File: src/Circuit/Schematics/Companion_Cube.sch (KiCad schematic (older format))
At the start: 13 parts

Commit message: Better origins on models
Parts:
- added D?: LED, ~, symbol LED
- added R?: R, ~, symbol R
- C?: value 10uF -> 1uF
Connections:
- net GND: now also R?.1
- net VCC: now also D?.1 (A)
- new net: D?.2 (K), R?.2
- no-connect marks 0 -> 3
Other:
- moved on the sheet: C?, CON?, IC?, P?, R?, RG?, U?

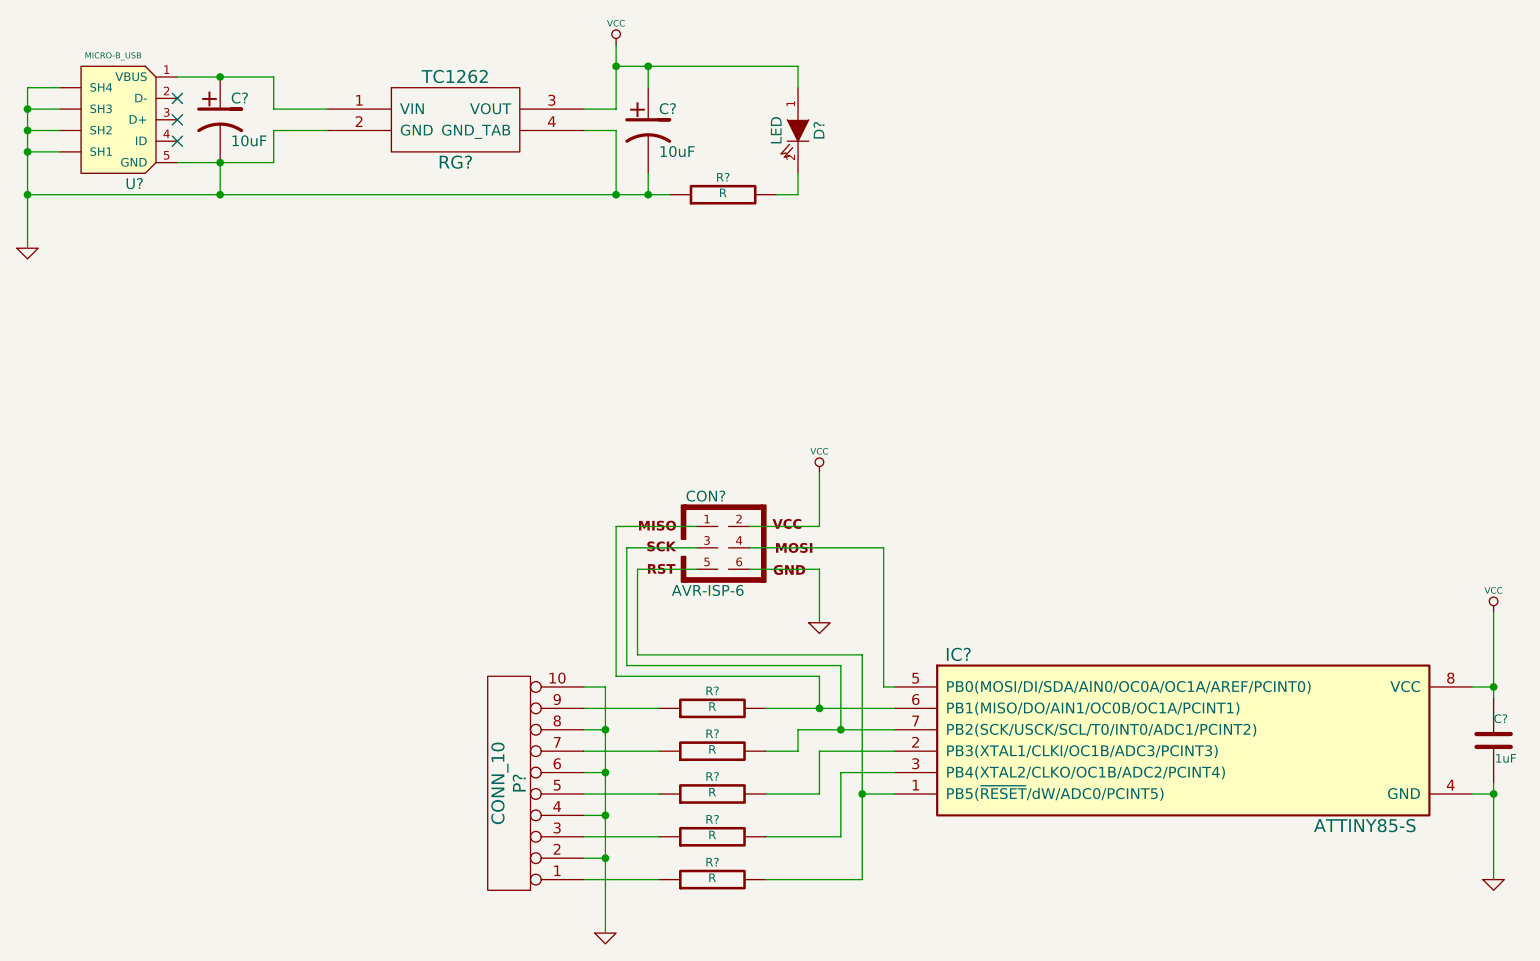
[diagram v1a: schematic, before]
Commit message: Removed use of reset pin from LED controller
The walls of the lid have also been shortened for slightly quicker
printing.
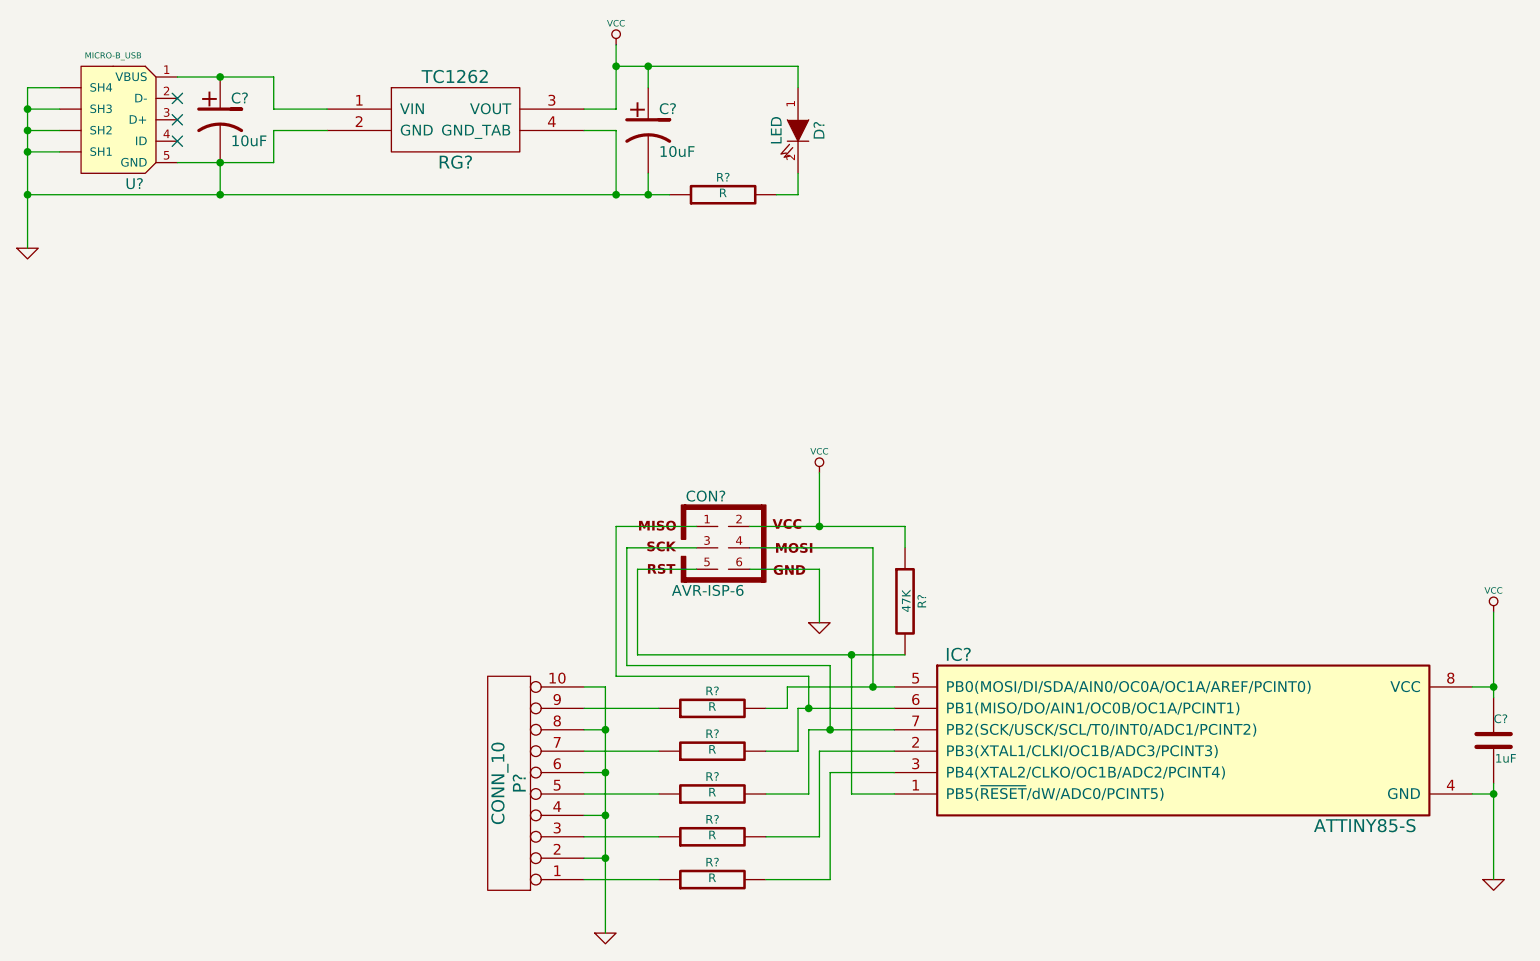
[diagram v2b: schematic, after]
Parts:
- added R?: 47K, ~, symbol R
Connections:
- net VCC: now also R?.1
- net at CON?.5, IC?.1 (PB5(~RESET~/dW/ADC0/PCINT5)): now also R?.2; no longer R?.2
- net at IC?.2 (PB3(XTAL1/CLKI/OC1B/ADC3/PCINT3)): now also R?.2; no longer R?.2
- net at IC?.3 (PB4(XTAL2/CLKO/OC1B/ADC2/PCINT4)): now also R?.2; no longer R?.2
- net at CON?.4, IC?.5 (PB0(MOSI/DI/SDA/AIN0/OC0A/OC1A/AREF/PCINT0)): now also R?.2
- net at CON?.1, IC?.6 (PB1(MISO/DO/AIN1/OC0B/OC1A/PCINT1)): now also R?.2; no longer R?.2
- net at CON?.3, IC?.7 (PB2(SCK/USCK/SCL/T0/INT0/ADC1/PCINT2)): now also R?.2; no longer R?.2
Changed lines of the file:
@@
 Sheet 1 1
 Title "noname.sch"
-Date "4 dec 2014"
+Date "5 dec 2014"
 Rev ""
 Comp ""
@@
 	0    1    1    0
 $EndComp
-Wire Wire Line
-	1100 1250 950  1250
-Wire Wire Line
-	950  1250 950  2000
-Wire Wire Line
-	1100 1350 950  1350
-Connection ~ 950  1350
-Wire Wire Line
-	1100 1450 950  1450
-Connection ~ 950  1450
-Wire Wire Line
-	1100 1550 950  1550
-Connection ~ 950  1550
-Wire Wire Line
-	950  1750 3950 1750
-Connection ~ 950  1750
-Wire Wire Line
-	5000 4550 4850 4550
-Wire Wire Line
-	4850 3900 4850 4950
-Wire Wire Line
-	4850 4950 4400 4950
-Wire Wire Line
-	3900 4950 3550 4950
-Wire Wire Line
-	5000 4450 4750 4450
-Wire Wire Line
-	4750 4450 4750 4750
-Wire Wire Line
-	4750 4750 4400 4750
-Wire Wire Line
-	3900 4750 3550 4750
-Wire Wire Line
-	5000 4350 4650 4350
-Wire Wire Line
-	4650 4350 4650 4550
-Wire Wire Line
-	4650 4550 4400 4550
-Wire Wire Line
-	3900 4550 3550 4550
-Wire Wire Line
-	4550 4250 5000 4250
-Wire Wire Line
-	4550 4250 4550 4350
-Wire Wire Line
-	4550 4350 4400 4350
-Wire Wire Line
-	3900 4350 3550 4350
-Wire Wire Line
-	4400 4150 5000 4150
-Wire Wire Line
-	3900 4150 3550 4150
-Wire Wire Line
-	3550 4050 3650 4050
-Wire Wire Line
-	3650 4050 3650 5200
-Wire Wire Line
-	3550 4850 3650 4850
-Connection ~ 3650 4850
-Wire Wire Line
-	3550 4650 3650 4650
-Connection ~ 3650 4650
-Wire Wire Line
-	3550 4450 3650 4450
-Connection ~ 3650 4450
-Wire Wire Line
-	3550 4250 3650 4250
-Connection ~ 3650 4250
-Wire Wire Line
-	7700 4550 7800 4550
-Wire Wire Line
-	7800 4500 7800 4950
-Wire Wire Line
-	7700 4050 7800 4050
-Wire Wire Line
-	7800 3700 7800 4100
-Wire Wire Line
-	4850 3900 3800 3900
-Wire Wire Line
-	3800 3900 3800 3500
-Wire Wire Line
-	3800 3500 4075 3500
-Connection ~ 4850 4550
-Wire Wire Line
-	4075 3400 3750 3400
-Wire Wire Line
-	3750 3400 3750 3950
-Wire Wire Line
-	3750 3950 4750 3950
-Wire Wire Line
-	4750 3950 4750 4250
-Connection ~ 4750 4250
-Wire Wire Line
-	4075 3300 3700 3300
-Wire Wire Line
-	3700 3300 3700 4000
-Wire Wire Line
-	3700 4000 4650 4000
-Wire Wire Line
-	4650 4000 4650 4150
-Connection ~ 4650 4150
-Wire Wire Line
-	5000 4050 4950 4050
-Wire Wire Line
-	4950 4050 4950 3400
-Wire Wire Line
-	4950 3400 4325 3400
-Wire Wire Line
-	4325 3500 4650 3500
-Wire Wire Line
-	4650 3500 4650 3750
-Wire Wire Line
-	4325 3300 4650 3300
-Wire Wire Line
-	4650 3300 4650 3050
-Connection ~ 7800 4550
-Connection ~ 7800 4050
-Wire Wire Line
-	2100 1200 2100 1350
-Wire Wire Line
-	2100 1350 2350 1350
-Wire Wire Line
-	2100 1600 2100 1450
-Wire Wire Line
-	2100 1450 2350 1450
-Wire Wire Line
-	3550 1350 3700 1350
-Wire Wire Line
-	3700 1350 3700 1050
-Wire Wire Line
-	3700 1750 3700 1450
-Wire Wire Line
-	3700 1450 3550 1450
-Wire Wire Line
-	1650 1200 2100 1200
-Connection ~ 1850 1200
-Wire Wire Line
-	1650 1600 2100 1600
-Connection ~ 1850 1600
-Wire Wire Line
-	1850 1600 1850 1750
-Connection ~ 1850 1750
-Wire Wire Line
-	3700 1150 4550 1150
-Connection ~ 3700 1150
 $Comp
 L R R?
@@
 	0    -1   -1   0
 $EndComp
+Connection ~ 3850 1150
+Wire Wire Line
+	3850 1250 3850 1150
+Connection ~ 3850 1750
+Wire Wire Line
+	3850 1750 3850 1650
+Connection ~ 3700 1750
+Wire Wire Line
+	4550 1750 4450 1750
+Wire Wire Line
+	4550 1650 4550 1750
 Wire Wire Line
 	4550 1150 4550 1250
-Wire Wire Line
-	4550 1650 4550 1750
-Wire Wire Line
-	4550 1750 4450 1750
-Connection ~ 3700 1750
-Wire Wire Line
-	3850 1650 3850 1750
-Connection ~ 3850 1750
-Wire Wire Line
-	3850 1250 3850 1150
-Connection ~ 3850 1150
+Connection ~ 3700 1150
+Wire Wire Line
+	3700 1150 4550 1150
+Connection ~ 1850 1750
+Wire Wire Line
+	1850 1600 1850 1750
+Connection ~ 1850 1600
+Wire Wire Line
+	1650 1600 2100 1600
+Connection ~ 1850 1200
+Wire Wire Line
+	1650 1200 2100 1200
+Wire Wire Line
+	3700 1450 3550 1450
+Wire Wire Line
+	3700 1750 3700 1450
+Wire Wire Line
+	3700 1050 3700 1350
+Wire Wire Line
+	3700 1350 3550 1350
+Wire Wire Line
+	2100 1450 2350 1450
+Wire Wire Line
+	2100 1600 2100 1450
+Wire Wire Line
+	2100 1350 2350 1350
+Wire Wire Line
+	2100 1200 2100 1350
+Connection ~ 7800 4050
+Connection ~ 7800 4550
+Wire Wire Line
+	4650 3300 4650 3050
+Wire Wire Line
+	4325 3300 5050 3300
+Wire Wire Line
+	4650 3500 4650 3750
+Wire Wire Line
+	4325 3500 4650 3500
+Wire Wire Line
+	4900 3400 4325 3400
+Wire Wire Line
+	3700 3300 3700 4000
+Wire Wire Line
+	4075 3300 3700 3300
+Wire Wire Line
+	3750 3400 3750 3950
+Wire Wire Line
+	4075 3400 3750 3400
+Wire Wire Line
+	3800 3500 4075 3500
+Wire Wire Line
+	3800 3900 3800 3500
+Wire Wire Line
+	7800 3700 7800 4100
+Wire Wire Line
+	7700 4050 7800 4050
+Wire Wire Line
+	7800 4500 7800 4950
+Wire Wire Line
+	7700 4550 7800 4550
+Connection ~ 3650 4250
+Wire Wire Line
+	3550 4250 3650 4250
+Connection ~ 3650 4450
+Wire Wire Line
+	3650 4450 3550 4450
+Connection ~ 3650 4650
+Wire Wire Line
+	3650 4650 3550 4650
+Connection ~ 3650 4850
+Wire Wire Line
+	3650 4850 3550 4850
+Wire Wire Line
+	3650 4050 3650 5200
+Wire Wire Line
+	3550 4050 3650 4050
+Wire Wire Line
+	3900 4150 3550 4150
+Wire Wire Line
+	3900 4350 3550 4350
+Wire Wire Line
+	3900 4550 3550 4550
+Wire Wire Line
+	3900 4750 3550 4750
+Wire Wire Line
+	3900 4950 3550 4950
+Connection ~ 950  1750
+Wire Wire Line
+	950  1750 3950 1750
+Connection ~ 950  1550
+Wire Wire Line
+	950  1550 1100 1550
+Connection ~ 950  1450
+Wire Wire Line
+	950  1450 1100 1450
+Connection ~ 950  1350
+Wire Wire Line
+	1100 1350 950  1350
+Wire Wire Line
+	950  1250 950  2000
+Wire Wire Line
+	1100 1250 950  1250
+Wire Wire Line
+	5000 4050 4500 4050
+Wire Wire Line
+	4500 4050 4500 4150
+Wire Wire Line
+	4500 4150 4400 4150
+Wire Wire Line
+	5000 4150 4550 4150
+Wire Wire Line
+	4550 4150 4550 4350
+Wire Wire Line
+	4550 4350 4400 4350
+Wire Wire Line
+	5000 4250 4600 4250
+Wire Wire Line
+	4600 4250 4600 4550
+Wire Wire Line
+	4600 4550 4400 4550
+Wire Wire Line
+	5000 4350 4650 4350
+Wire Wire Line
+	4650 4350 4650 4750
+Wire Wire Line
+	4650 4750 4400 4750
+Wire Wire Line
+	5000 4450 4700 4450
+Wire Wire Line
+	4700 4450 4700 4950
+Wire Wire Line
+	4700 4950 4400 4950
+Wire Wire Line
+	5000 4550 4800 4550
+Wire Wire Line
+	4800 4550 4800 3900
+Wire Wire Line
+	3800 3900 5050 3900
+Wire Wire Line
+	4900 3400 4900 4050
+Connection ~ 4900 4050
+Wire Wire Line
+	3750 3950 4700 3950
+Wire Wire Line
+	4700 3950 4700 4250
+Connection ~ 4700 4250
+Wire Wire Line
+	3700 4000 4600 4000
+Wire Wire Line
+	4600 4000 4600 4150
+Connection ~ 4600 4150
+$Comp
+L R R?
+U 1 1 54818E36
+P 5050 3650
+F 0 "R?" V 5130 3650 40  0000 C CNN
+F 1 "47K" V 5057 3651 40  0000 C CNN
+F 2 "~" V 4980 3650 30  0000 C CNN
+F 3 "~" H 5050 3650 30  0000 C CNN
+	1    5050 3650
+	1    0    0    -1
+$EndComp
+Connection ~ 4800 3900
+Wire Wire Line
+	5050 3300 5050 3400
+Connection ~ 4650 3300
 $EndSCHEMATC

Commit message: Added button schematic
The button will be on a separate PCB so that it can be placed at the
other side of the cube.

The button includes a capacitor for debounce and an extra resistor as a
precaution, incase the button is ever connected to an output*.

*Should be safe for up to 5v, passing 20ma which is pretty common for
MCU I/O. Requires atleast a 1/10W dissipation.
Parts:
- removed P?: CONN_10, ~, symbol CONN_10
- removed R?: R, ~, symbol R
- removed R?: 47K, ~, symbol R
- added P?: CONN_11, ~, symbol CONN_11
- added R?: 47K, ~, symbol R
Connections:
- net GND: now also P?.10 (P10), P?.2 (P2), P?.4 (P4), P?.6 (P6), P?.8 (P8)
- net VCC: now also P?.11 (P11), R?.1
- net at CON?.5, IC?.1 (PB5(~RESET~/dW/ADC0/PCINT5)): now also R?.2
- net at CON?.4, IC?.5 (PB0(MOSI/DI/SDA/AIN0/OC0A/OC1A/AREF/PCINT0)): now also P?.9 (P9)
- net at R?.1: now also P?.1 (P1)
- net at R?.1: now also P?.3 (P3)
- net at R?.1: now also P?.5 (P5)
- net at R?.1: now also P?.7 (P7)
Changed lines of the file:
@@
-$EndComp
-$Comp
-L CONN_10 P?
-U 1 1 54803D48
-P 3200 4500
-F 0 "P?" V 3150 4500 60  0000 C CNN
-F 1 "CONN_10" V 3250 4500 60  0000 C CNN
-F 2 "~" H 3200 4500 60  0000 C CNN
-F 3 "~" H 3200 4500 60  0000 C CNN
-	1    3200 4500
-	-1   0    0    1
 $EndComp
 $Comp
@@
 $EndComp
 $Comp
-L R R?
-U 1 1 54803F6F
-P 4150 4150
-F 0 "R?" V 4230 4150 40  0000 C CNN
-F 1 "R" V 4157 4151 40  0000 C CNN
-F 2 "~" V 4080 4150 30  0000 C CNN
-F 3 "~" H 4150 4150 30  0000 C CNN
-	1    4150 4150
-	0    -1   -1   0
-$EndComp
-$Comp
 L GND #PWR?
 U 1 1 5480417C
@@
 L VCC #PWR?
 U 1 1 54804A55
-P 4650 3050
-F 0 "#PWR?" H 4650 3150 30  0001 C CNN
-F 1 "VCC" H 4650 3150 30  0000 C CNN
-F 2 "~" H 4650 3050 60  0000 C CNN
-F 3 "~" H 4650 3050 60  0000 C CNN
-	1    4650 3050
+P 4650 2950
+F 0 "#PWR?" H 4650 3050 30  0001 C CNN
+F 1 "VCC" H 4650 3050 30  0000 C CNN
+F 2 "~" H 4650 2950 60  0000 C CNN
+F 3 "~" H 4650 2950 60  0000 C CNN
+	1    4650 2950
 	1    0    0    -1
 $EndComp
@@
 Connection ~ 3700 1150
 Wire Wire Line
-	3700 1150 4550 1150
+	3700 1150 3850 1150
+Wire Wire Line
+	3850 1150 4550 1150
 Connection ~ 1850 1750
 Wire Wire Line
@@
 Connection ~ 1850 1600
 Wire Wire Line
-	1650 1600 2100 1600
+	1650 1600 1850 1600
+Wire Wire Line
+	1850 1600 2100 1600
 Connection ~ 1850 1200
 Wire Wire Line
-	1650 1200 2100 1200
+	1650 1200 1850 1200
+Wire Wire Line
+	1850 1200 2100 1200
 Wire Wire Line
 	3700 1450 3550 1450
@@
 	3700 1750 3700 1450
 Wire Wire Line
-	3700 1050 3700 1350
+	3700 1050 3700 1150
+Wire Wire Line
+	3700 1150 3700 1350
 Wire Wire Line
 	3700 1350 3550 1350
@@
 Connection ~ 7800 4550
 Wire Wire Line
-	4650 3300 4650 3050
-Wire Wire Line
-	4325 3300 5050 3300
+	4650 3300 4650 3100
+Wire Wire Line
+	4650 3100 4650 2950
+Wire Wire Line
+	4325 3300 4650 3300
+Wire Wire Line
+	4650 3300 5050 3300
 Wire Wire Line
 	4650 3500 4650 3750
@@
 	3800 3900 3800 3500
 Wire Wire Line
-	7800 3700 7800 4100
+	7800 3700 7800 4050
+Wire Wire Line
+	7800 4050 7800 4100
 Wire Wire Line
 	7700 4050 7800 4050
 Wire Wire Line
-	7800 4500 7800 4950
+	7800 4500 7800 4550
+Wire Wire Line
+	7800 4550 7800 4950
 Wire Wire Line
 	7700 4550 7800 4550
 Connection ~ 3650 4250
 Wire Wire Line
-	3550 4250 3650 4250
+	3450 4250 3650 4250
 Connection ~ 3650 4450
 Wire Wire Line
-	3650 4450 3550 4450
+	3450 4450 3650 4450
 Connection ~ 3650 4650
 Wire Wire Line
-	3650 4650 3550 4650
+	3450 4650 3650 4650
 Connection ~ 3650 4850
 Wire Wire Line
-	3650 4850 3550 4850
-Wire Wire Line
-	3650 4050 3650 5200
-Wire Wire Line
-	3550 4050 3650 4050
-Wire Wire Line
-	3900 4150 3550 4150
-Wire Wire Line
-	3900 4350 3550 4350
-Wire Wire Line
-	3900 4550 3550 4550
-Wire Wire Line
-	3900 4750 3550 4750
-Wire Wire Line
-	3900 4950 3550 4950
+	3450 4850 3650 4850
+Wire Wire Line
+	3650 4050 3650 4250
+Wire Wire Line
+	3650 4250 3650 4450
+Wire Wire Line
+	3650 4450 3650 4650
+Wire Wire Line
+	3650 4650 3650 4850
+Wire Wire Line
+	3650 4850 3650 5200
+Wire Wire Line
+	3450 4050 3650 4050
+Wire Wire Line
+	3450 4150 4500 4150
+Wire Wire Line
+	3450 4350 3900 4350
+Wire Wire Line
+	3450 4550 3900 4550
+Wire Wire Line
+	3450 4750 3900 4750
+Wire Wire Line
+	3450 4950 3900 4950
 Connection ~ 950  1750
 Wire Wire Line
-	950  1750 3950 1750
+	950  1750 1850 1750
+Wire Wire Line
+	1850 1750 3700 1750
+Wire Wire Line
+	3700 1750 3850 1750
+Wire Wire Line
+	3850 1750 3950 1750
 Connection ~ 950  1550
 Wire Wire Line
@@
 	1100 1350 950  1350
 Wire Wire Line
-	950  1250 950  2000
+	950  1250 950  1350
+Wire Wire Line
+	950  1350 950  1450
+Wire Wire Line
+	950  1450 950  1550
+Wire Wire Line
+	950  1550 950  1750
+Wire Wire Line
+	950  1750 950  2000
 Wire Wire Line
 	1100 1250 950  1250
 Wire Wire Line
-	5000 4050 4500 4050
+	5000 4050 4900 4050
+Wire Wire Line
+	4900 4050 4500 4050
 Wire Wire Line
 	4500 4050 4500 4150
 Wire Wire Line
-	4500 4150 4400 4150
-Wire Wire Line
-	5000 4150 4550 4150
+	5000 4150 4600 4150
+Wire Wire Line
+	4600 4150 4550 4150
 Wire Wire Line
 	4550 4150 4550 4350
@@
 	4550 4350 4400 4350
 Wire Wire Line
-	5000 4250 4600 4250
+	5000 4250 4700 4250
+Wire Wire Line
+	4700 4250 4600 4250
 Wire Wire Line
 	4600 4250 4600 4550
@@
 	4800 4550 4800 3900
 Wire Wire Line
-	3800 3900 5050 3900
+	3800 3900 4800 3900
+Wire Wire Line
+	4800 3900 5050 3900
 Wire Wire Line
 	4900 3400 4900 4050
@@
 	4600 4000 4600 4150
 Connection ~ 4600 4150
-$Comp
-L R R?
-U 1 1 54818E36
-P 5050 3650
-F 0 "R?" V 5130 3650 40  0000 C CNN
-F 1 "47K" V 5057 3651 40  0000 C CNN
-F 2 "~" V 4980 3650 30  0000 C CNN
-F 3 "~" H 5050 3650 30  0000 C CNN
-	1    5050 3650
-	1    0    0    -1
-$EndComp
 Connection ~ 4800 3900
-Wire Wire Line
-	5050 3300 5050 3400
 Connection ~ 4650 3300
+$Comp
+L R R?
+U 1 1 54818FB5
+P 5050 3600
+F 0 "R?" V 5130 3600 40  0000 C CNN
+F 1 "47K" V 5057 3601 40  0000 C CNN
+F 2 "~" V 4980 3600 30  0000 C CNN
+F 3 "~" H 5050 3600 30  0000 C CNN
+	1    5050 3600
+	1    0    0    -1
+$EndComp
+Wire Wire Line
+	5050 3900 5050 3850
+Wire Wire Line
+	5050 3300 5050 3350
+$Comp
+L CONN_11 P?
+U 1 1 54819F28
+P 3100 4450
+F 0 "P?" V 3050 4450 60  0000 C CNN
+F 1 "CONN_11" V 3150 4450 60  0000 C CNN
+F 2 "~" H 3100 4450 60  0000 C CNN
+F 3 "~" H 3100 4450 60  0000 C CNN
+	1    3100 4450
+	-1   0    0    1
+$EndComp
+Wire Wire Line
+	3450 3950 3650 3950
+Wire Wire Line
+	3650 3950 3650 3100
+Wire Wire Line
+	3650 3100 4650 3100
+Connection ~ 4650 3100
 $EndSCHEMATC

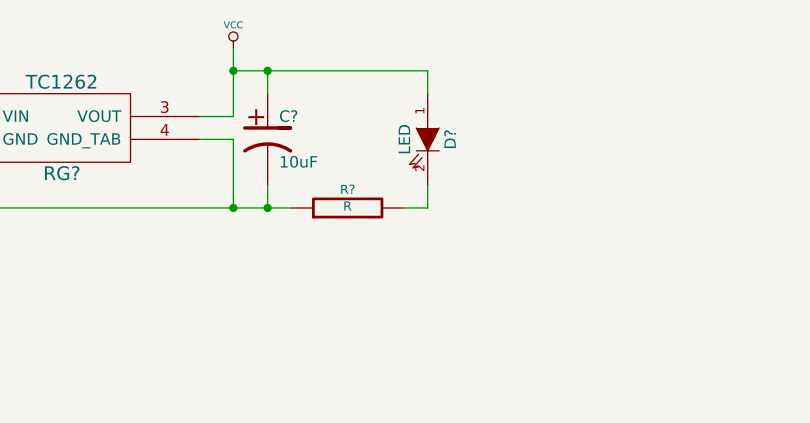
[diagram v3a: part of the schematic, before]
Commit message: Changes to cube model.
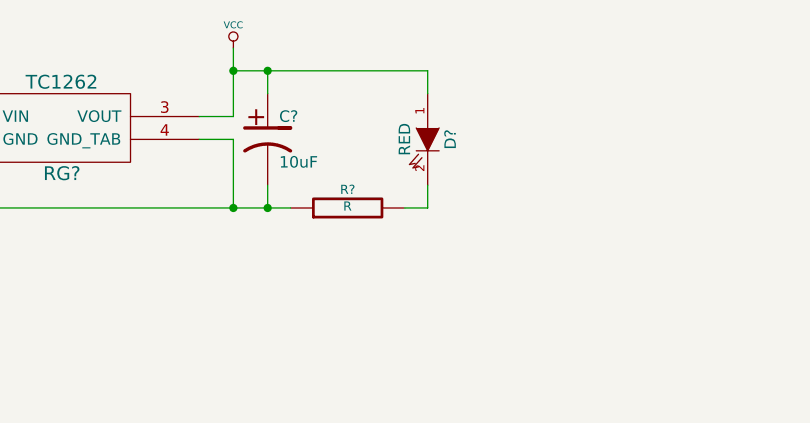
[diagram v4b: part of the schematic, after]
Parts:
- D?: value LED -> RED
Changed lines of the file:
@@
 P 4550 1450
 F 0 "D?" H 4550 1550 50  0000 C CNN
-F 1 "LED" H 4550 1350 50  0000 C CNN
+F 1 "RED" H 4550 1350 50  0000 C CNN
 F 2 "~" H 4550 1450 60  0000 C CNN
 F 3 "~" H 4550 1450 60  0000 C CNN
